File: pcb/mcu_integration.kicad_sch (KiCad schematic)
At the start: 24 parts, among them J1 Micro_SD_Card, J3 Conn_01x06, SW1 RST_SW, U1 STM32F103RBTx, U2 MCP3301, U3 REF192, Y2 8MHz

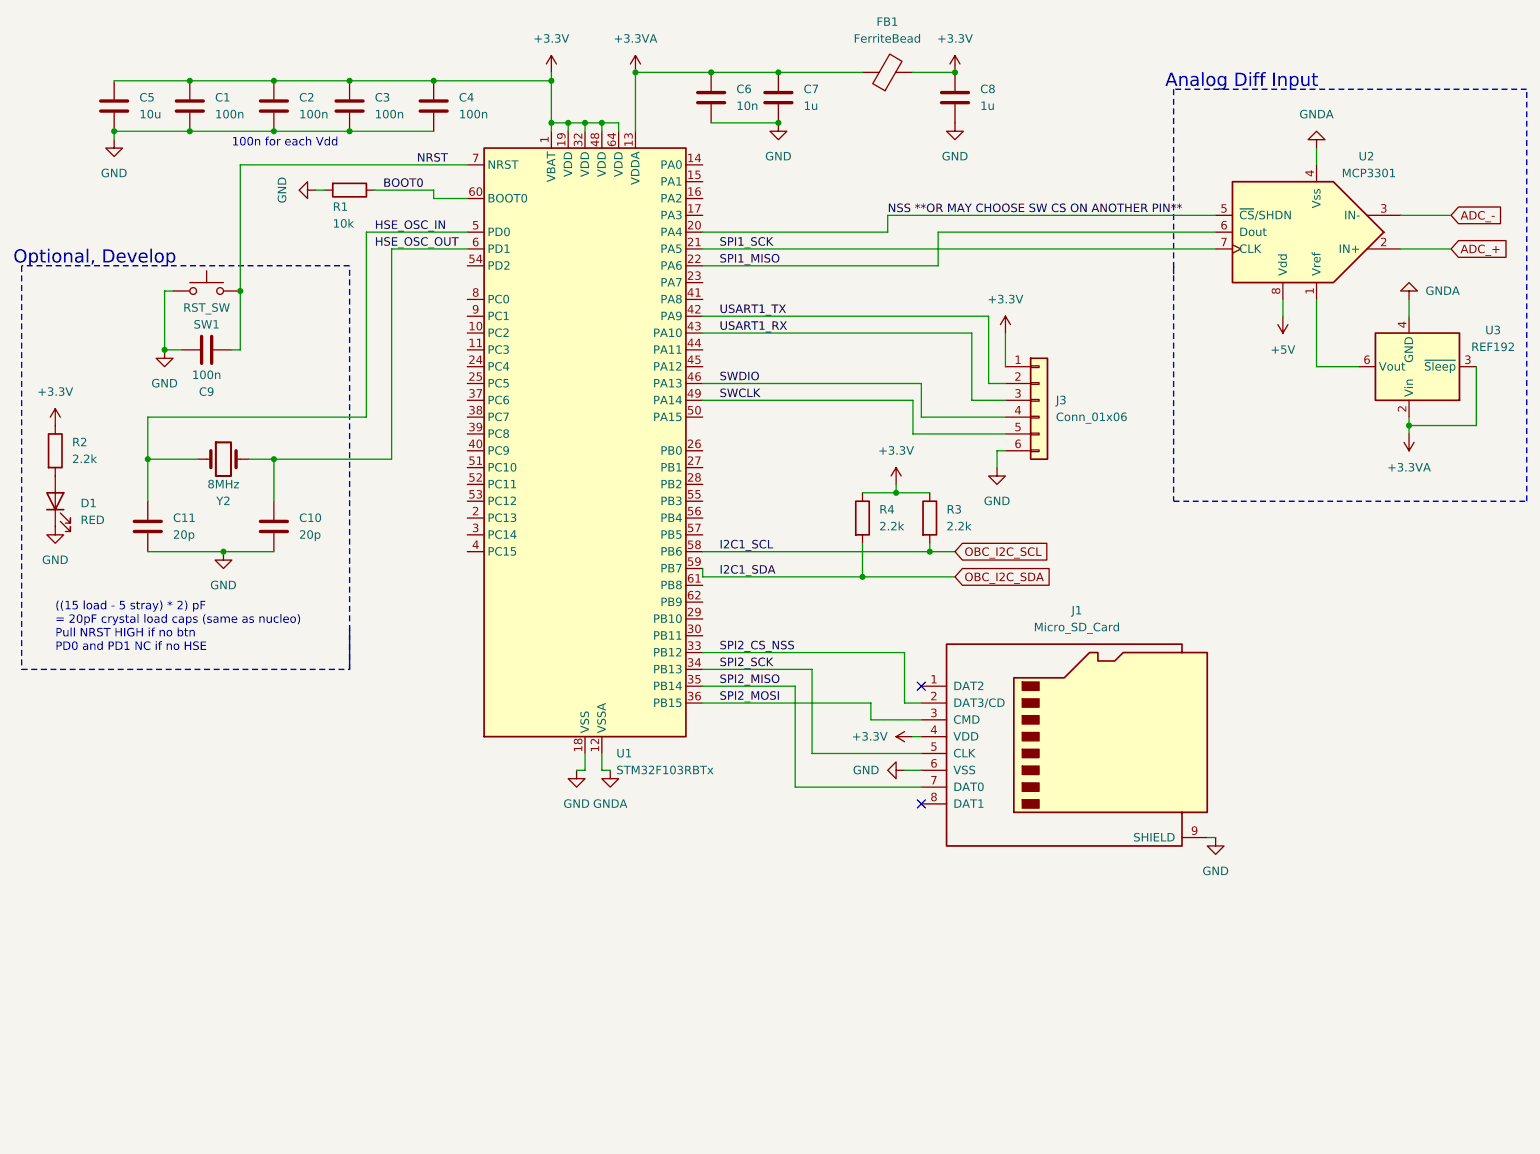
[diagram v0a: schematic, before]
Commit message: mcu integration done, 10x10cm pcb+micro sd+osc
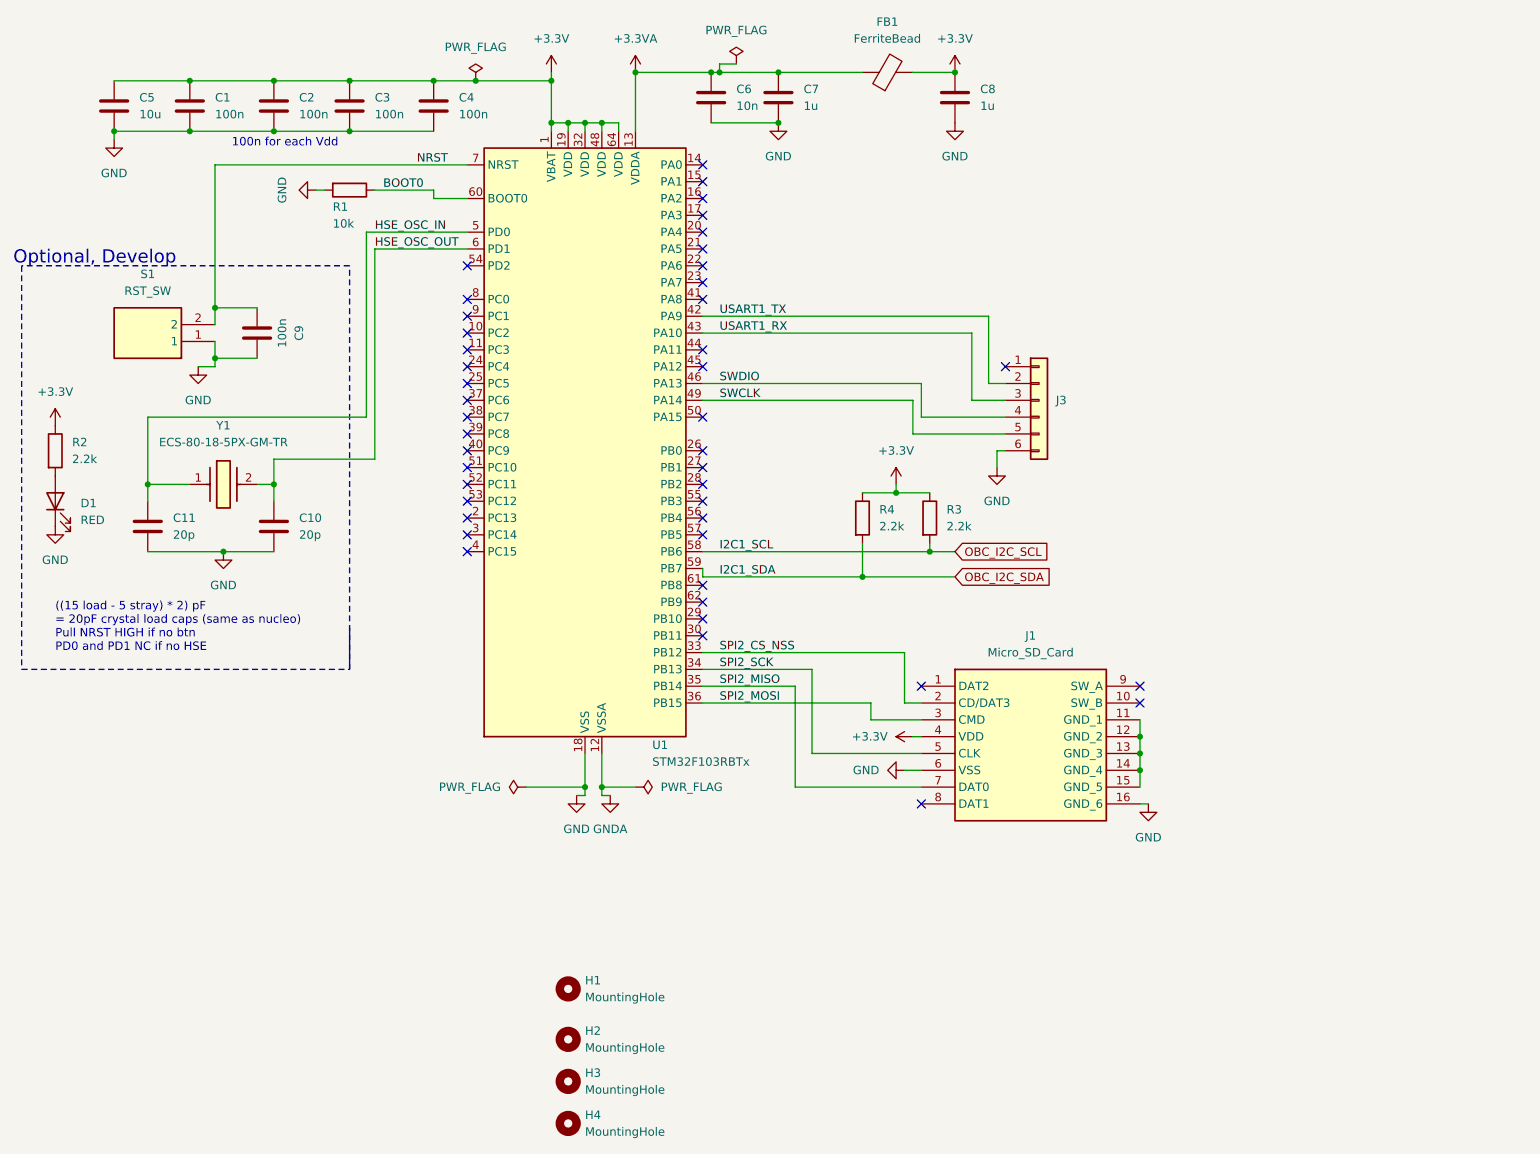
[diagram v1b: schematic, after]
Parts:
- removed SW1: RST_SW, symbol Switch:SW_Push
- removed U2: MCP3301, symbol Analog_ADC:MCP3301
- removed U3: REF192, symbol Reference_Voltage:REF192
- removed Y2: 8MHz, symbol Device:Crystal
- added H1, H2, H3, H4: MountingHole, MountingHole:MountingHole_2.2mm_M2, symbol Mechanical:MountingHole
- added S1: RST_SW, capstone:95C04A3GWRT, symbol capstone:95C04A3GWRT
- added Y1: ECS-80-18-5PX-GM-TR, capstone:ECS80185PXGMTR, symbol capstone:ECS-80-18-5PX-GM-TR
- C1, C10, C11, C2, C3, C4, C6, C7, C8, C9: footprint (none) -> Capacitor_SMD:C_0402_1005Metric
- C5: footprint (none) -> Capacitor_SMD:C_0603_1608Metric
- D1: footprint (none) -> LED_SMD:LED_0603_1608Metric
- FB1: footprint (none) -> Inductor_SMD:L_0603_1608Metric
- J1: footprint (none) -> 22017781; symbol Connector:Micro_SD_Card -> capstone:2201778-1; Height (none) -> 1.95; Manufacturer_Name (none) -> TE Connectivity; Manufacturer_Part_Number (none) -> 2201778-1; Mouser Part Number (none) -> 571-2201778-1; Mouser Price/Stock (none) -> https://www.mouser.co.uk/ProductDetail/TE-Connectivity/2201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
- J3: footprint (none) -> Connector_PinHeader_2.54mm:PinHeader_1x06_P2.54mm_Horizontal
- R1, R2, R3, R4: footprint (none) -> Resistor_SMD:R_0402_1005Metric
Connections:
- net +3.3V: no longer J3.1 (Pin_1)
- net GND: now also J1.16 (GND_6), S1.1; no longer J1.9 (SHIELD)
- net HSE_OSC_IN: now also Y1.1
- net HSE_OSC_OUT: now also C10.1, U1.6 (PD1), Y1.2
- net NRST: now also S1.2
- net NSS **OR MAY CHOOSE SW CS ON ANOTHER PIN**: no longer names the net of U1.20 (PA4)
- net SPI1_MISO: no longer names the net of U1.22 (PA6)
- net SPI1_SCK: no longer names the net of U1.21 (PA5)
- new net: J1.11 (GND_1), J1.12 (GND_2), J1.13 (GND_3), J1.14 (GND_4), J1.15 (GND_5)
- no-connect marks 2 -> 44
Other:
- note removed: "Analog Diff Input"
- moved on the sheet: C9

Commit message: Signal gen and - 5 V circuits added
I added the two circuits for signal gen and - 5 V all capacitators are speced and in the #links in discord.
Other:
- added sheet Evan -5V and signal gen (Evan_-5V_and_signal_gen.kicad_sch)
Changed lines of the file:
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@@
-    (effects (font (size 1.27 1.27)) (justify left bottom))
-  )
-  (label "I2C1_SDA" (at 119.38 99.06 0) (fields_autoplaced)
     (effects (font (size 1.27 1.27)) (justify left bottom))
   )
@@
   )
   (label "USART1_RX" (at 119.38 62.23 0) (fields_autoplaced)
-    (effects (font (size 1.27 1.27)) (justify left bottom))
-  )
-  (label "I2C1_SCL" (at 119.38 95.25 0) (fields_autoplaced)
     (effects (font (size 1.27 1.27)) (justify left bottom))
   )
@@
       )
     )
+  )
+  (sheet (at 331.47 6.35) (size 331.47 200.66) (fields_autoplaced)
+    (stroke (width 0.1524) (type solid))
+    (fill (color 0 0 0 0.0000))
+    (property "Sheetname" "Evan -5V and signal gen" (at 331.47 5.6384 0)
+      (effects (font (size 1.27 1.27)) (justify left bottom))
+    )
+    (property "Sheetfile" "Evan_-5V_and_signal_gen.kicad_sch" (at 331.47 207.5946 0)
+      (effects (font (size 1.27 1.27)) (justify left top))
+    )
+    (instances
+      (project "mcu_integration"
+        (path "/c0210bc3-f67f-47d8-a34e-f002a728adb2" (page "2"))
+      )
+    )

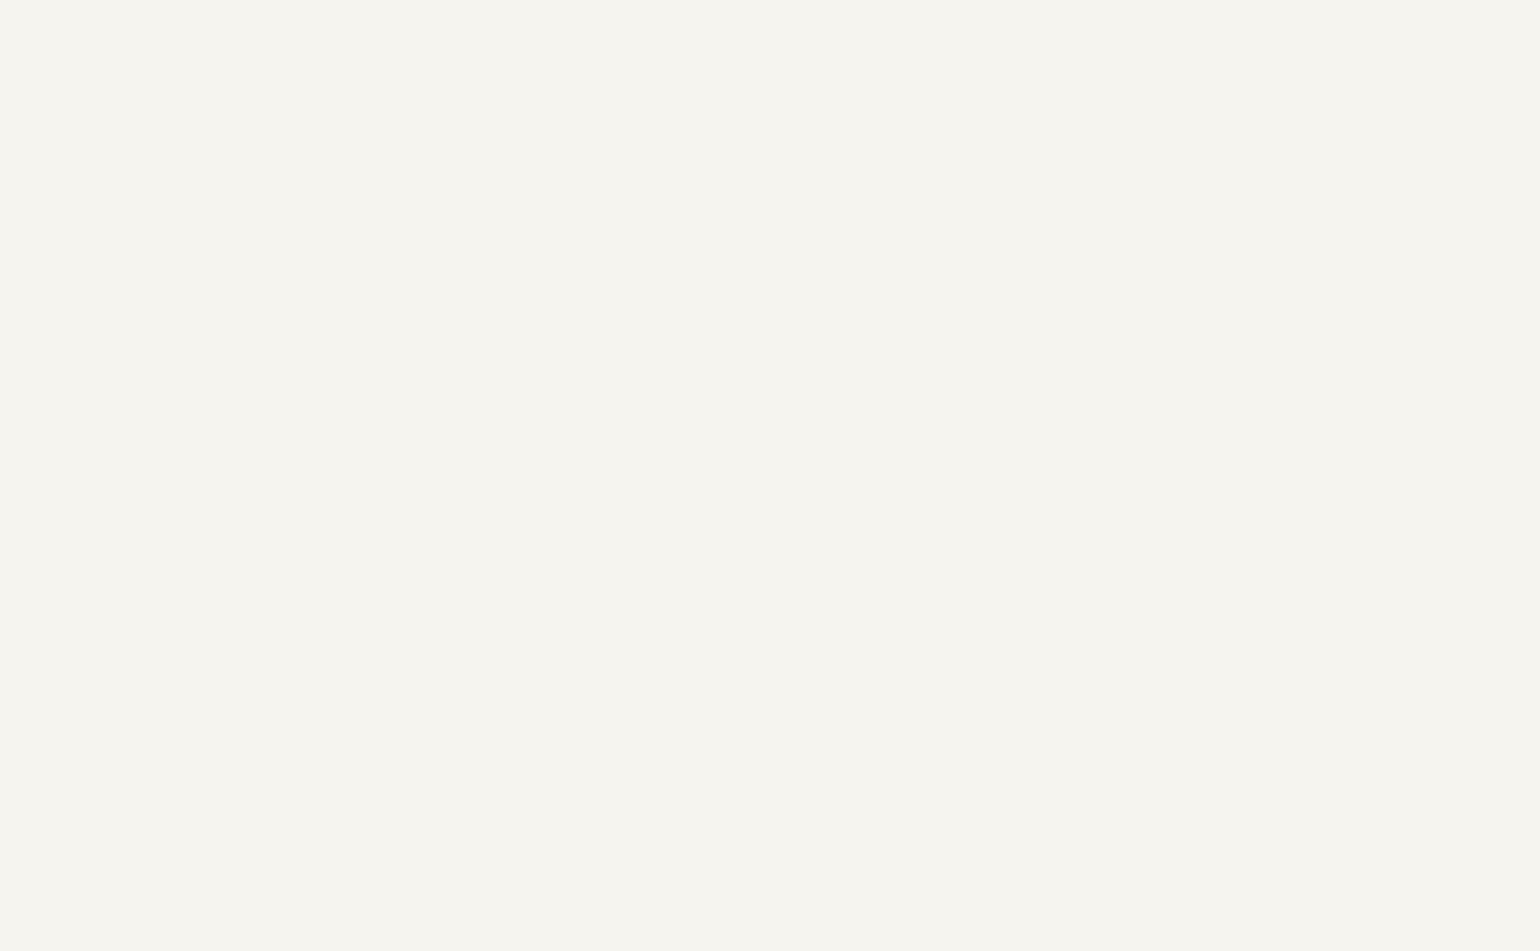
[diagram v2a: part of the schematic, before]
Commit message: Implemented IC Test portion (AD844, FOD814, REF192)
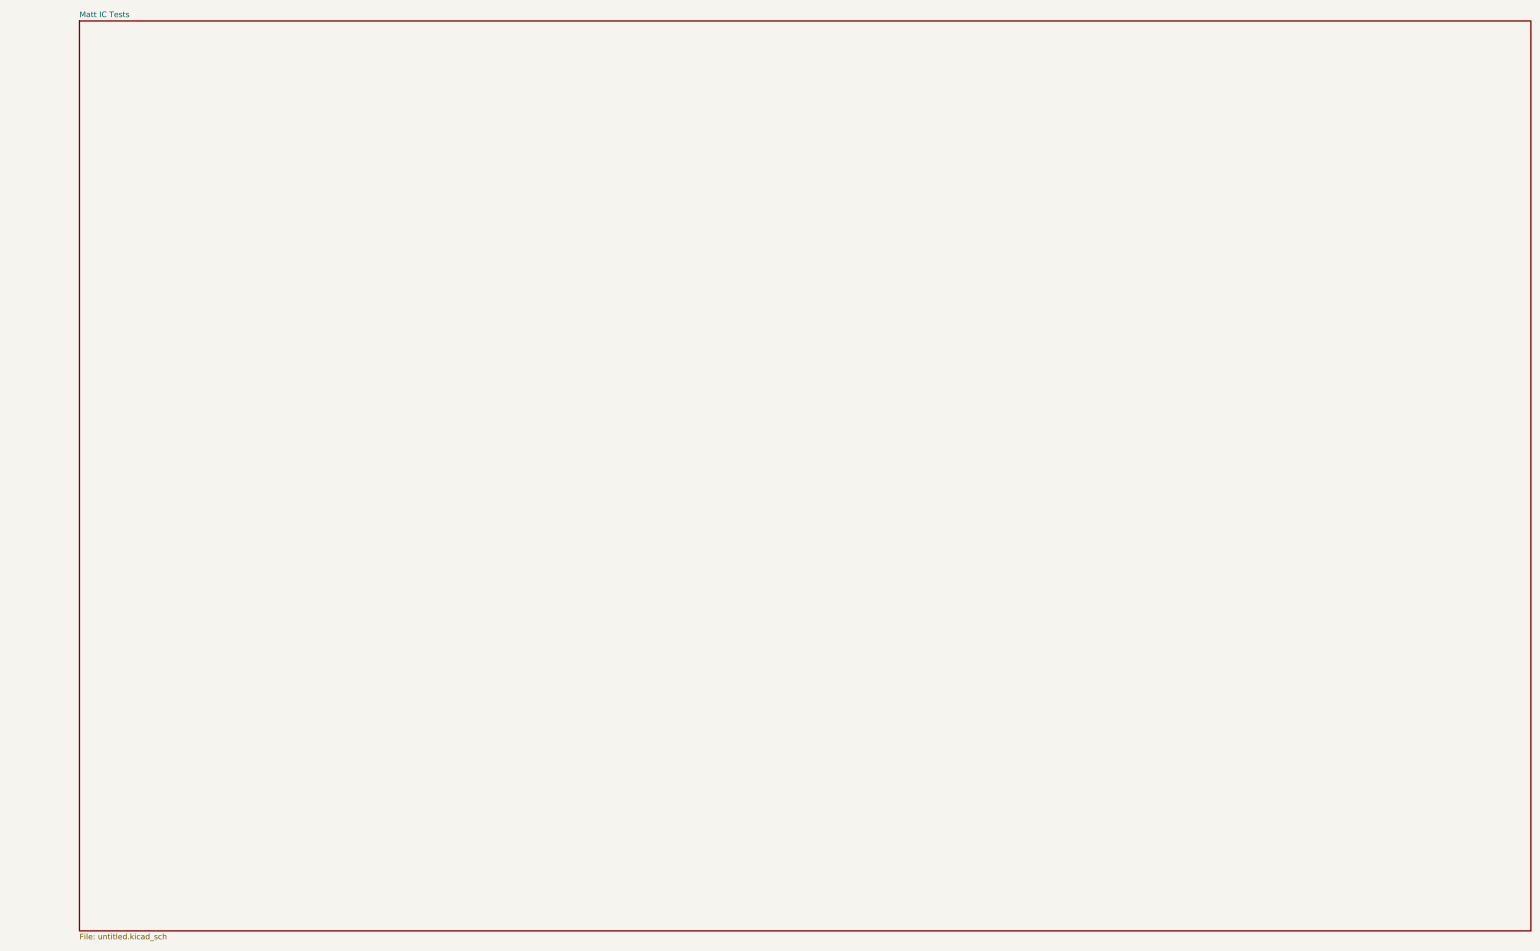
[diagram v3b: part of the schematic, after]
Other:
- added sheet Matt IC Tests (untitled.kicad_sch)
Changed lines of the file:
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@@
+    )
+  )
+  (sheet (at 698.5 0) (size 330.2 207.01) (fields_autoplaced)
+    (stroke (width 0.1524) (type solid))
+    (fill (color 0 0 0 0.0000))
+    (property "Sheetname" "Matt IC Tests" (at 698.5 -0.7116 0)
+      (effects (font (size 1.27 1.27)) (justify left bottom))
+    )
+    (property "Sheetfile" "untitled.kicad_sch" (at 698.5 207.5946 0)
+      (effects (font (size 1.27 1.27)) (justify left top))
+    )
+    (instances
+      (project "mcu_integration"
+        (path "/c0210bc3-f67f-47d8-a34e-f002a728adb2" (page "3"))
+      )
     )
   )

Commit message: Added labels for ADC's, change R's and C's values to have more of same parts (#7)
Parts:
- C6: value 10n -> 100n
- R1: value 10k -> 2.2k
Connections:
- net ADC1_IN12_OPTO_F_MEL: now reaches U1.10 (PC2)
- net ADC1_IN13_OPTO_C_MEL: now reaches U1.11 (PC3)
- net ADC1_IN0_SINE: now reaches U1.14 (PA0)
- net ADC1_IN1_OPAMP_UNSHD: now reaches U1.15 (PA1)
- net ADC1_IN2_OPAMP_MEL: now reaches U1.16 (PA2)
- net ADC1_IN3_OPAMP_AL: now reaches U1.17 (PA3)
- net ADC1_IN4_VREF_UNSHD: now reaches U1.20 (PA4)
- net ADC1_IN5_VREF_MEL: now reaches U1.21 (PA5)
- net ADC1_IN6_VREF_AL: now reaches U1.22 (PA6)
- net ADC1_IN7_VREG_NOSHD: now reaches U1.23 (PA7)
- net ADC1_IN14_OPTO_F_AL: now reaches U1.24 (PC4)
- net ADC1_IN15_OPTO_C_AL: now reaches U1.25 (PC5)
- net ADC1_IN8_VREG_MEL: now reaches U1.26 (PB0)
- net ADC1_IN9_VREG_AL: now reaches U1.27 (PB1)
- net ADC1_IN10_OPTO_F_NOSHD: now reaches U1.8 (PC0)
- net ADC1_IN11_OPTO_C_NOSHD: now reaches U1.9 (PC1)
- no-connect marks 44 -> 28
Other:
- note added: "LC Low Pass"
- moved on the sheet: C6, C7, C8, FB1

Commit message: first bulk commit of routing
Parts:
- J1: footprint 22017781 -> (none)
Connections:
- net GND: now also J1.11 (GND_1), J1.12 (GND_2), J1.13 (GND_3), J1.14 (GND_4), J1.15 (GND_5)
- net +3.3V renamed 3.3V Output
- net +3.3VA: no longer names the net of C6.1, C7.1, FB1.1, U1.13 (VDDA)
- net ADC1_IN11_OPTO_C_NOSHD renamed ADC1_IN11_OPTO_E_NOSHD
- net ADC1_IN13_OPTO_C_MEL renamed ADC1_IN13_OPTO_E_MEL
- net ADC1_IN15_OPTO_C_AL renamed ADC1_IN15_OPTO_E_AL
- net ADC1_IN1_OPAMP_UNSHD renamed ADC1_IN1_OPAMP_NOSHD
- net ADC1_IN4_VREF_UNSHD renamed ADC1_IN4_VREF_NOSHD

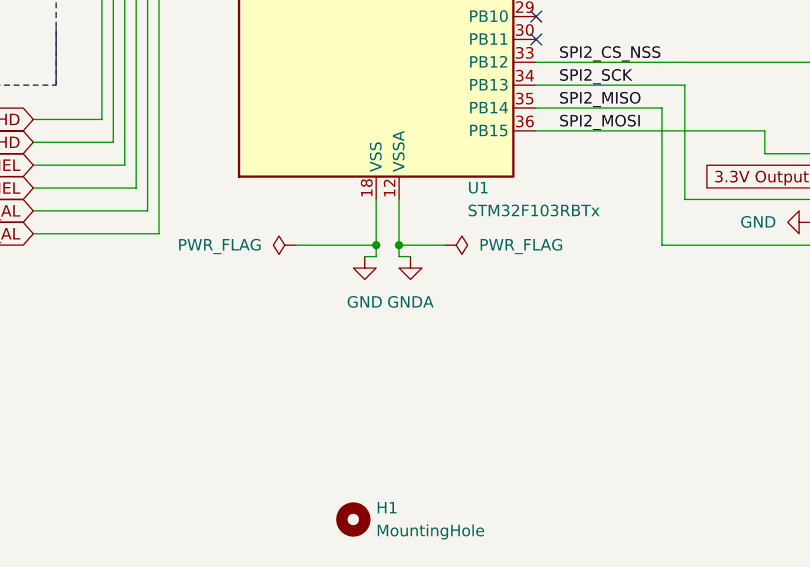
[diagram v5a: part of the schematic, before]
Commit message: removed about 300 warnings
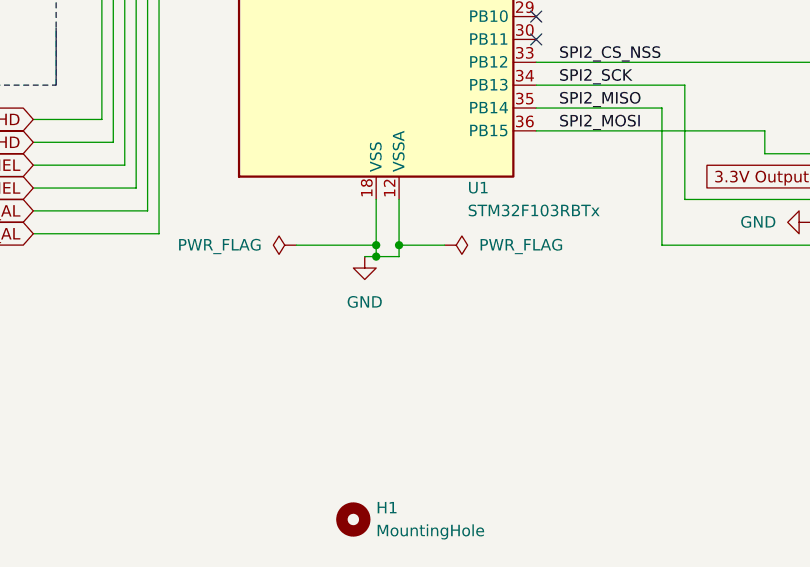
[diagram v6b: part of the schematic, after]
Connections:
- net GNDA is gone; now on net GND: U1.12 (VSSA)
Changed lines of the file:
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@@
   (junction (at 82.55 24.13) (diameter 0) (color 0 0 0 0)
+  )
+  (junction (at 99.06 132.08) (diameter 0) (color 0 0 0 0)
   )
   (junction (at 128.27 20.32) (diameter 0) (color 0 0 0 0)
@@
     (stroke (width 0) (type default))
   )
-  (wire (pts (xy 102.87 132.08) (xy 101.6 132.08))
-    (stroke (width 0) (type default))
-  )
   (wire (pts (xy 60.96 124.46) (xy 72.39 124.46))
     (stroke (width 0) (type default))
@@
   )
   (wire (pts (xy 116.84 82.55) (xy 119.38 82.55))
+    (stroke (width 0) (type default))
+  )
+  (wire (pts (xy 99.06 132.08) (xy 101.6 132.08))
     (stroke (width 0) (type default))
   )
@@
         )
       )
-    )
-  )
-  (symbol (lib_id "power:GNDA") (at 102.87 132.08 0) (unit 1)
-    (in_bom yes) (on_board yes) (dnp no) (fields_autoplaced)
-    (property "Reference" "#PWR09" (at 102.87 138.43 0)
-      (effects (font (size 1.27 1.27)) hide)
-    )
-    (property "Value" "GNDA" (at 102.87 137.16 0)
-      (effects (font (size 1.27 1.27)))
-    )
-    (property "Footprint" "" (at 102.87 132.08 0)
-      (effects (font (size 1.27 1.27)) hide)
-    )
-    (property "Datasheet" "" (at 102.87 132.08 0)
-      (effects (font (size 1.27 1.27)) hide)
-    )
-    (pin "1")
-    (instances
-      (project "mcu_integration"
-        (path "/c0210bc3-f67f-47d8-a34e-f002a728adb2"
-          (reference "#PWR09") (unit 1)
-        )
-      )
